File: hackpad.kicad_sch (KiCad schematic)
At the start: 4 parts, among them SW1 SW_Push, SW2 SW_Push, SW3 SW_Push, U1 MOUDLE-SEEEDUINO-XIAO

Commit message: made the schematic myself
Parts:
- removed SW1, SW2, SW3: SW_Push, Button_Switch_Keyboard:SW_Cherry_MX_1.00u_PCB, symbol Switch:SW_Push
- added D1, D2, D3, D4, D5, D6, D7: 1N914, Diode_THT:D_DO-35_SOD27_P7.62mm_Horizontal, symbol Diode:1N914
- added D2, D8, D9: SK6812MINI-E, LED_SMD:LED_SK6812MINI-E_3.2x2.8mm_P1.5mm_ReverseMount, symbol LED:SK6812MINI-E
- added J1: Conn_01x04, symbol Connector_Generic:Conn_01x04
- added SW1, SW2, SW3, SW4, SW5, SW6: SW_Push_45deg, symbol Switch:SW_Push_45deg
- added SW4: RotaryEncoder_Switch, symbol Device:RotaryEncoder_Switch
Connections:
- net GND: now also D2.1 (VSS), D8.1 (VSS), D9.1 (VSS), J1.4 (Pin_4), SW4.C
- net EC11A: now reaches U1.9 (PA7_A8_D8_SCK)
- net EC11A: now also SW4.A
- net LEDPIN: now reaches U1.11 (PA6_A10_D10_MOSI)
- net LEDPIN: now also D8.2 (DIN)
- net Column 1: now reaches U1.1 (PA02_A0_D0)
- net Column 1: now also SW1.1, SW2.1
- net Row 2: now reaches U1.10 (PA5_A9_D9_MISO)
- net Row 2: now also D1.1 (K), D2.1 (K), D3.1 (K)
- net VCC: now reaches U1.14 (5V)
- net VCC: now also D2.3 (VDD), D8.3 (VDD), D9.3 (VDD), J1.3 (Pin_3)
- net Column 2: now reaches U1.2 (PA4_A1_D1)
- net Column 2: now also SW3.1, SW4.1
- net Column 3: now reaches U1.3 (PA10_A2_D2)
- net Column 3: now also SW5.1, SW6.1
- net Column 4: now reaches U1.4 (PA11_A3_D3)
- net SDA: now reaches U1.5 (PA8_A4_D4_SDA)
- net SDA: now also J1.2 (Pin_2)
- net SCL: now reaches U1.6 (PA9_A5_D5_SCL)
- net SCL: now also J1.1 (Pin_1)
- net Row 1: now reaches U1.7 (PB08_A6_D6_TX)
- net Row 1: now also D4.1 (K), D5.1 (K), D6.1 (K), D7.1 (K)
- net EC11B: now reaches U1.8 (PB09_A7_D7_RX)
- net EC11B: now also SW4.B
- new net: D1.2 (A), SW2.2
- new net: D4.2 (A), SW1.2
- new net: D8.4 (DOUT), D9.2 (DIN)
- new net: D2.2 (DIN), D9.4 (DOUT)
- new net: D6.2 (A), SW5.2
- new net: D3.2 (A), SW6.2
- new net: D5.2 (A), SW3.2
- new net: D2.2 (A), SW4.2
- new net  Column 4: SW4.S1
- new net EC11SWA: D7.2 (A), SW4.S2

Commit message: fixed the schematics
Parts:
- J1: footprint (none) -> Connector_PinHeader_2.54mm:PinHeader_1x04_P2.54mm_Vertical
- SW1, SW2, SW3, SW5, SW6: footprint (none) -> Button_Switch_Keyboard:SW_Cherry_MX_1.00u_PCB
- SW4: footprint (none) -> Rotary_Encoder:RotaryEncoder_Alps_EC11E-Switch_Vertical_H20mm
- SW9: renamed from SW4; footprint (none) -> Button_Switch_Keyboard:SW_Cherry_MX_1.00u_PCB
- renumbered D2 to D22, D4 to D99
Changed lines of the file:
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@@
 			)
 		)
-		(property "Footprint" ""
+		(property "Footprint" "Button_Switch_Keyboard:SW_Cherry_MX_1.00u_PCB"
 			(at 149.86 77.47 0)
 			(hide yes)
@@
 			)
 		)
-		(property "Footprint" ""
+		(property "Footprint" "Button_Switch_Keyboard:SW_Cherry_MX_1.00u_PCB"
 			(at 149.86 48.26 0)
 			(hide yes)
@@
 		(dnp no)
 		(fields_autoplaced yes)
-		(property "Reference" "D4"
+		(property "Reference" "D99"
 			(at 154.94 53.3399 90)
 			(show_name no)
@@
 			(project "hackpad"
 				(path "/31f34989-3700-4e7f-abb0-845b2d2b8d31"
-					(reference "D4")
+					(reference "D99")
 					(unit 1)
 				)
@@
 			)
 		)
-		(property "Footprint" ""
+		(property "Footprint" "Button_Switch_Keyboard:SW_Cherry_MX_1.00u_PCB"
 			(at 199.39 48.26 0)
 			(hide yes)
@@
 			)
 		)
-		(property "Footprint" ""
+		(property "Footprint" "Connector_PinHeader_2.54mm:PinHeader_1x04_P2.54mm_Vertical"
 			(at 148.59 115.57 0)
 			(hide yes)
@@
 			)
 		)
-		(property "Footprint" ""
+		(property "Footprint" "Button_Switch_Keyboard:SW_Cherry_MX_1.00u_PCB"
 			(at 199.39 76.2 0)
 			(hide yes)
@@
 			)
 		)
-		(property "Footprint" ""
+		(property "Footprint" "Button_Switch_Keyboard:SW_Cherry_MX_1.00u_PCB"
 			(at 173.99 48.26 0)
 			(hide yes)
@@
 		(dnp no)
 		(fields_autoplaced yes)
-		(property "Reference" "SW4"
+		(property "Reference" "SW9"
 			(at 173.99 68.58 0)
 			(show_name no)
@@
 			)
 		)
-		(property "Footprint" ""
+		(property "Footprint" "Button_Switch_Keyboard:SW_Cherry_MX_1.00u_PCB"
 			(at 173.99 76.2 0)
 			(hide yes)
@@
 			(project "hackpad"
 				(path "/31f34989-3700-4e7f-abb0-845b2d2b8d31"
-					(reference "SW4")
+					(reference "SW9")
 					(unit 1)
 				)
@@
 			)
 		)
-		(property "Footprint" ""
+		(property "Footprint" "Rotary_Encoder:RotaryEncoder_Alps_EC11E-Switch_Vertical_H20mm"
 			(at 111.76 116.586 0)
 			(hide yes)
@@
 		(dnp no)
 		(fields_autoplaced yes)
-		(property "Reference" "D2"
+		(property "Reference" "D22"
 			(at 179.07 81.2799 90)
 			(show_name no)
@@
 			(project "hackpad"
 				(path "/31f34989-3700-4e7f-abb0-845b2d2b8d31"
-					(reference "D2")
-					(unit 1)
-				)
+					(reference "D22")
+					(unit 1)
+				)

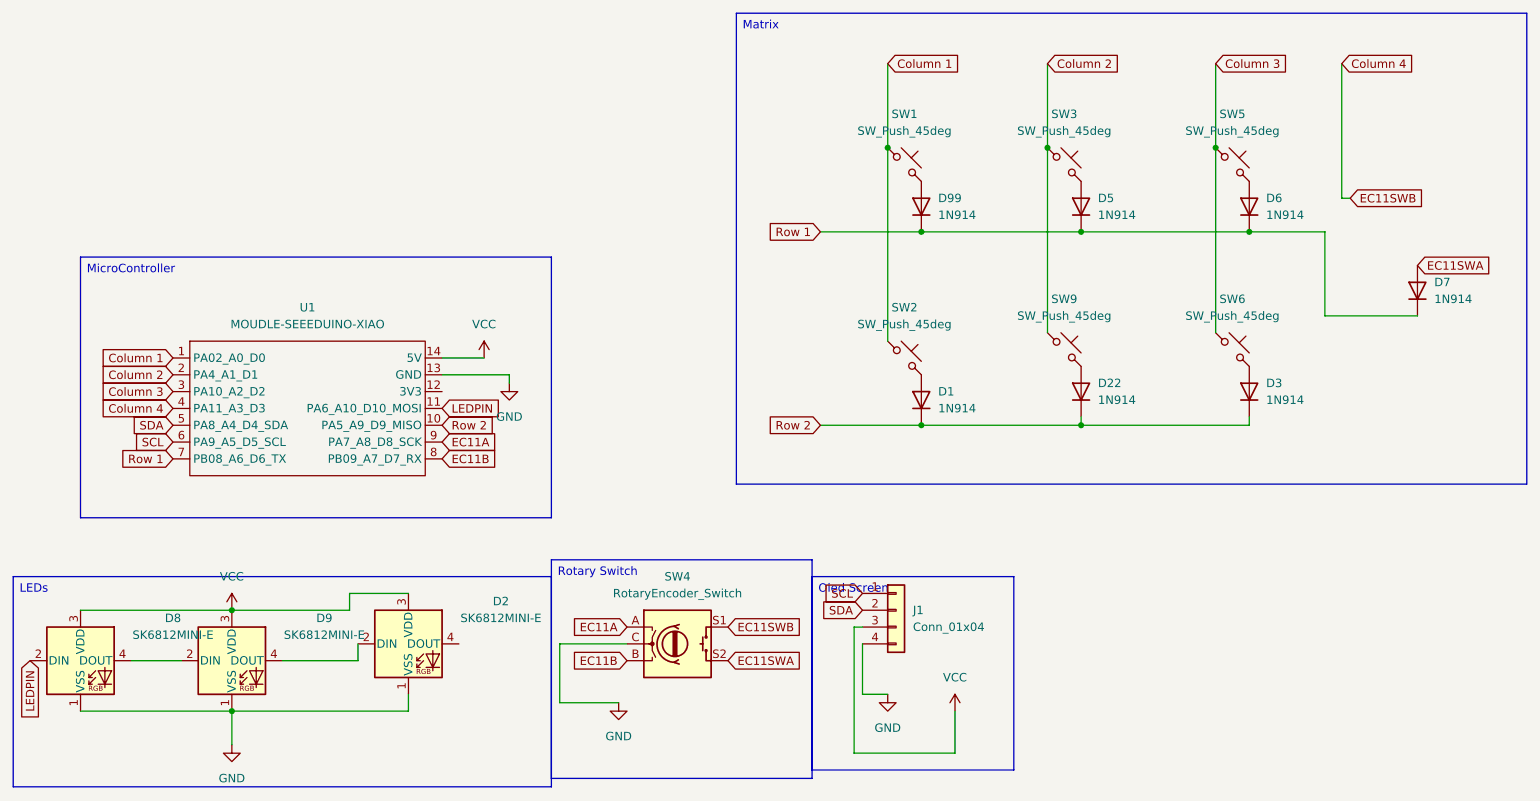
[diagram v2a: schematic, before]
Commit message: Completed the pcb and added 2 extra leds in the schematic !
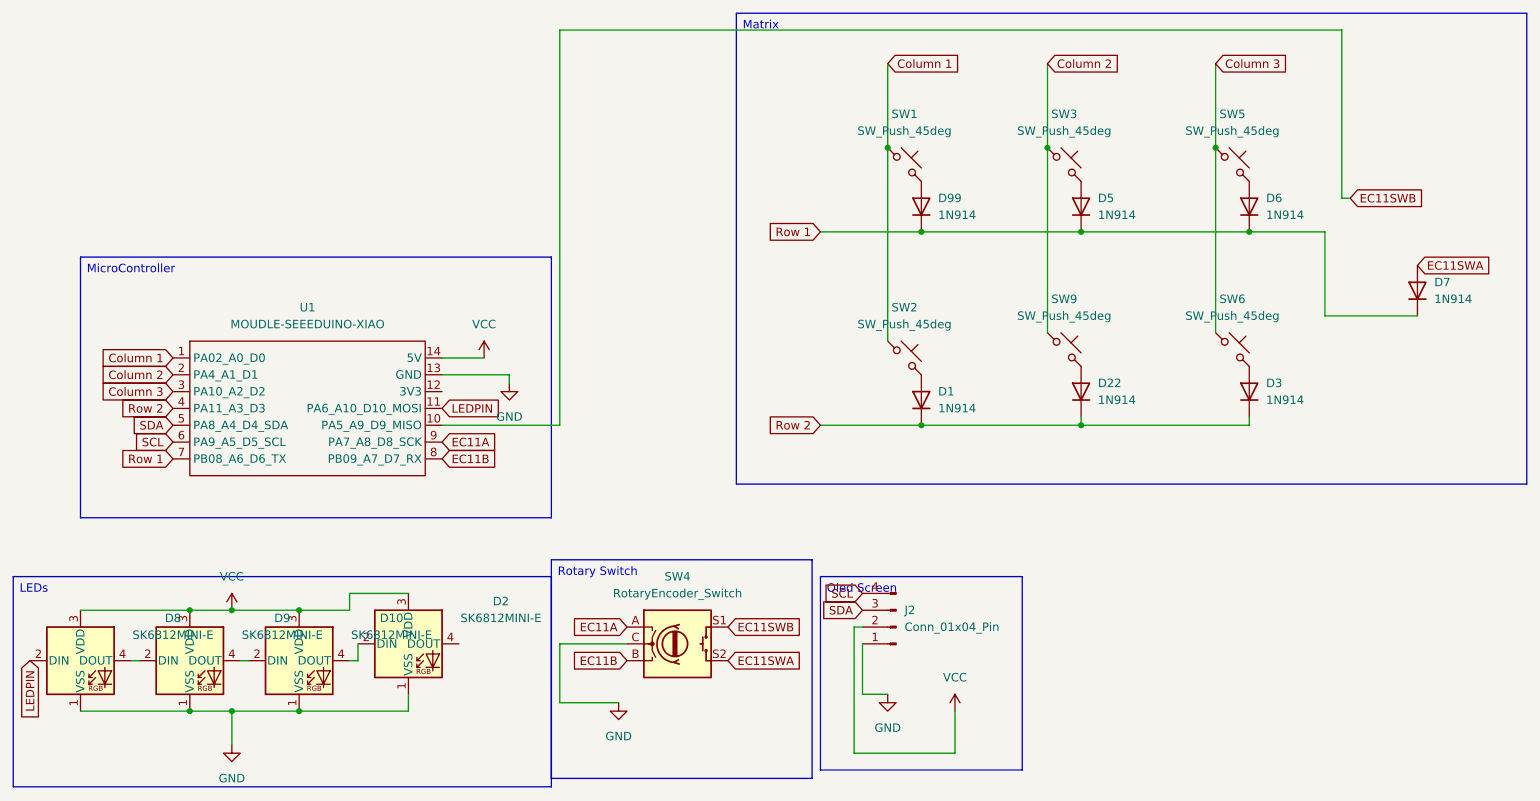
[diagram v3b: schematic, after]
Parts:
- removed J1: Conn_01x04, Connector_PinHeader_2.54mm:PinHeader_1x04_P2.54mm_Vertical, symbol Connector_Generic:Conn_01x04
- added D10: SK6812MINI-E, LED_SMD:LED_SK6812MINI-E_3.2x2.8mm_P1.5mm_ReverseMount, symbol LED:SK6812MINI-E
- added J2: Conn_01x04_Pin, Connector_PinHeader_2.54mm:PinHeader_1x04_P2.54mm_Vertical, symbol Connector:Conn_01x04_Pin
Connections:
- net Column 4 is gone; now on net Row 2: U1.4 (PA11_A3_D3)
- net GND: now also D10.1 (VSS), J2.1 (Pin_1)
- net Row 2: no longer U1.10 (PA5_A9_D9_MISO)
- net SCL: now also J2.4 (Pin_4)
- net SDA: now also J2.3 (Pin_3)
- net VCC: now also D10.3 (VDD), J2.2 (Pin_2)
- net at D9.4 (DOUT): now also D10.2 (DIN); no longer D2.2 (DIN)
- net  Column 4 renamed EC11SWB
- net EC11SWB: now also U1.10 (PA5_A9_D9_MISO)
- new net: D10.4 (DOUT), D2.2 (DIN)
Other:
- moved on the sheet: D9
